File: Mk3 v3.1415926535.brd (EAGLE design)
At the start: 121.6 x 70 mm, 152 parts, among them IC1 TPD3E001DRL, IC2 TPS62082, IC3 STM32F401V, IC4 BQ24092, IC6 CC3100MOD, IC7 BQ2970, IC8 LSM6DS3, IC9 LIS3MDL, J1 ZX62-AB-5PA(11), J2 ER-CON50HT-1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

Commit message: Sponsor logos to rear Note this moves the files to Eagle 7
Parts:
- removed LOGO3: MICROPYTHON-SILK, TiLDA Mk3 Parts:UPYTHON_LOGO_SLIKONLY
- removed U$5: (no value), TiLDA Mk3 Parts:EMFLOGO1
- added U$11: (no value), TiLDA Mk3 Parts:LOGO_MICROPYTHON_8MM
- added U$2: (no value), TiLDA Mk3 Parts:LOGO_MS_4MM
- added U$4: (no value), TiLDA Mk3 Parts:LOGO_ST_4MM
- added U$8: (no value), TiLDA Mk3 Parts:LOGO_TI_4MM
- added U$9: (no value), TiLDA Mk3 Parts:LOGO_HDC_4MM
- moved LOGO1 69.6 mm to (113.9, 49.2)
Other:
- board text added: "Made in the UK"
- board text added: "badge.emfcamp.org/2016"
- board text added: "v3.1415926535"
- board text removed: "MFB"
- board text removed: "Tilda Mk3 Rev.3 May 2016"

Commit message: Lots of clean up in schematic
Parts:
- C27, C5, C6: device passives-7351:C0805-N -> TiLDA Mk3 Parts:C0805-N
- D1: device SparkFun-LED:WS2812B -> TiLDA Mk3 Parts:WS2812B
- D2, D3: device Diodes:SOD123 -> TiLDA Mk3 Parts:SOD123
- IC3: value STM32F401V -> STM32L475VG
- J3: value SWD_SHROUD-PINHEAD -> 2x5 1.27mm
- JP1, JP2: device SparkFun-Connectors:1X11 -> TiLDA Mk3 Parts:1X11
- JP4: device tag-connect:TC2030-MCP-NL -> TiLDA Mk3 Parts:TC2030-MCP-NL
- LED2, LED4, LED5: value RED -> 0603 RED
- LED3: value GREEN -> 0603 GREEN
- LOGO2: value (none) -> LOGO_TI-4MM
- LOGO3: value (none) -> LOGO_ST-4MM
- LOGO4: value (none) -> LOGO_HCD-4MM
- LOGO5: value (none) -> LOGO_MICROSOFT-4MM
- LOGO6: value (none) -> LOGO_MICROPYTHON-8MM
- R7: value DNP or 0 -> DNP or 0603/0R/5%
- S1: value (none) -> 6x3; device SparkFun-Electromechanical:TACTILE-SWITCH-1101NE -> TiLDA Mk3 Parts:TACTILE-SWITCH-1101NE
- S3, S4: value 1217769 -> SKPMAPE010
- S7: value SWITCH-MOMENTARY-2SMD-1101NE -> 6x3; device SparkFun-Electromechanical:TACTILE-SWITCH-1101NE -> TiLDA Mk3 Parts:TACTILE-SWITCH-1101NE
- S8: value DNP -> DNP (6x3); device SparkFun-Electromechanical:TACTILE-SWITCH-1101NE -> TiLDA Mk3 Parts:TACTILE-SWITCH-1101NE
- SJ1: value JUMPER-PAD-2-NOYES_SILK -> SOLDERJUMPERNO; device SparkFun-Passives:PAD-JUMPER-2-NO_YES_SILK -> TiLDA Mk3 Parts:SJ_2S-NO
- renumbered U$11 to LOGO6, U$2 to LOGO5, U$4 to LOGO3, U$8 to LOGO2, U$9 to LOGO4
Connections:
- net BOOT0 renamed BOOT0/JOY_CEN
- net N$1 renamed DRDY
- net N$22 renamed C1
- net N$38 renamed VACP2
- net BTN_MENU: now also S7.P$2; no longer S7.2
- net CC_RST: now also S8.P$1; no longer S8.1
- net GND: now also S1.P$2, S7.P$1, S8.P$2; no longer S1.2, S7.1, S8.2
- net NRST: now also S1.P$1; no longer S1.1
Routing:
- net +3V3: track 547.7 -> 549.9 mm
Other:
- board text added: "designed and assembled in the UK"
- board text removed: "Made in the UK"

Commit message: More clean up
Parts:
- removed U$1: (no value), TiLDA Mk3 Parts:NAME_AREA
- IC6: value CC3100MOD -> CC3100MOD-LWK; device TiLDA Mk3 Parts:CC3100MOD -> TiLDA Mk3 Parts:CC3100MOD-LWK
- SW1: value JOYSTICK_MINI_MULTICOMP -> JOYSTICK_MINI_MULTICOM_NOSILK; device TiLDA Mk3 Parts:JOYSTICK_MULTICOMP -> TiLDA Mk3 Parts:JOYSTICK_MULTICOMP_NOSILK
- moved U2 54.0 mm to (89.2, 19.6), turned to 90 degrees
- moved FID2 31.3 mm to (121.5, 40.0)
- moved FID5 31.3 mm to (121.5, 40.0)
- moved FID3 29.7 mm to (30.0, -2.00)
- moved FID4 29.7 mm to (30.0, -2.00)
- moved FID1 24.7 mm to (71.5, 65.5)
- moved FID6 24.7 mm to (71.5, 65.5)
- moved IC6 12.6 mm to (104.7, 18.1)
- moved TP20 2.62 mm to (83.0, 20.5)
- moved ANT1 1.95 mm to (105.0, 1.60)
- moved R28 1.10 mm to (53.8, 48.1)
- moved Q4 0.91 mm to (52.5, 52.3)
- moved TP3 0.63 mm to (57.8, 38.6)
- moved C48 0.54 mm to (54.1, 58.1)
- moved D3 0.51 mm to (28.9, 46.5)
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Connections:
- net N$13 renamed BAT
- net N$2 renamed SW
- net N$50 renamed COUT
- net N$54 renamed VBAT_SWITCH_CONTROL
- net N$55 renamed DOUT
- net N$63 renamed V-
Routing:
- net GND: track 141.7 -> 131.4 mm
- net V_UNREG: track 350.9 -> 342.3 mm, vias 23 -> 22
- net FET_OUT: track 68.8 -> 72.5 mm
- net I2C_SDA: track 155.9 -> 153.7 mm
- net LCD0: track 50.7 -> 48.5 mm
- net I2C_SCL: track 156.3 -> 154.2 mm
- net N$64: track 15.7 -> 17.4 mm
- net +3V3: track 549.9 -> 548.3 mm
- net CC_RST: track 118.2 -> 119.6 mm
- net COUT: track 9.73 -> 10.9 mm
- net CC_IRQ: track 96.1 -> 95.1 mm
- net LCD_WRX: track 40.4 -> 41.2 mm
- net LCD_RD: track 40.8 -> 40.2 mm
- net SWDAT: track 56.8 -> 57.4 mm
- net BOOT0/JOY_CEN: track 149.0 -> 148.5 mm
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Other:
- board text removed: "MENU"

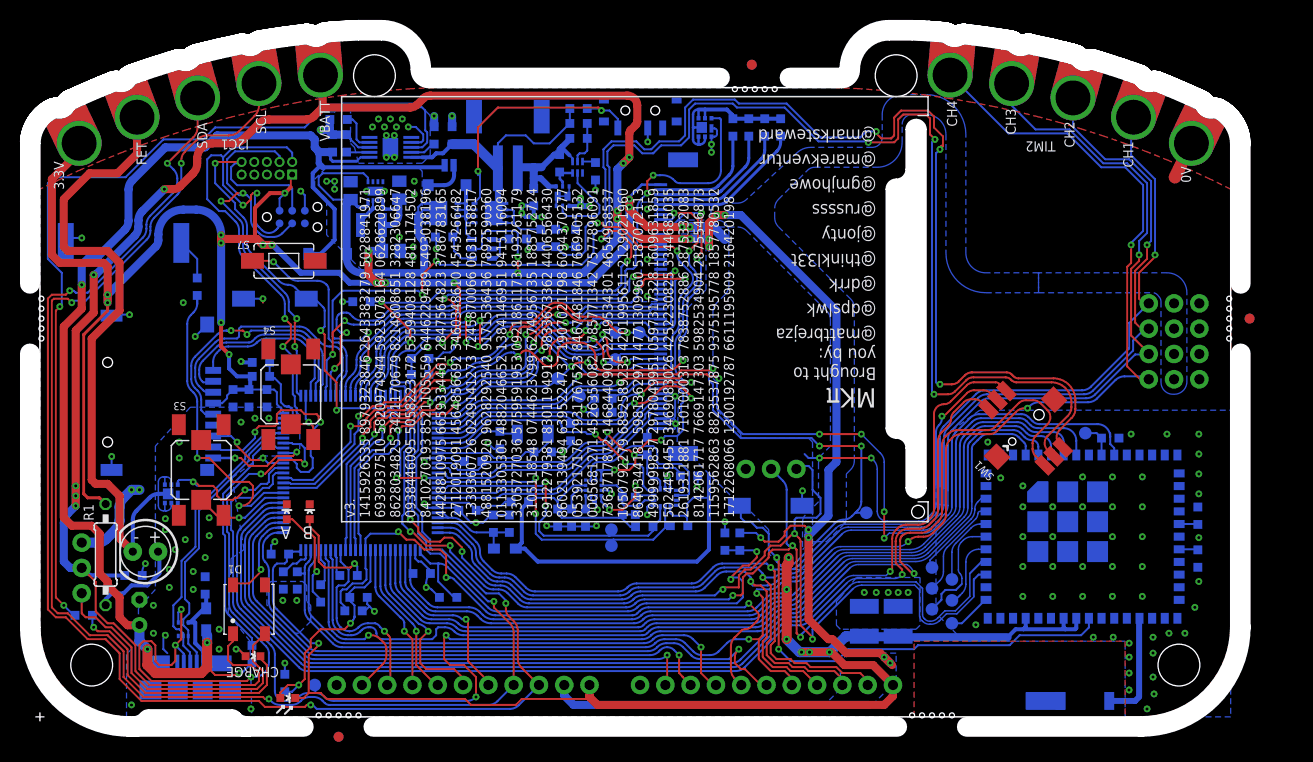
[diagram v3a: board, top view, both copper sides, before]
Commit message: Last footprint change and lots a trace clean up done
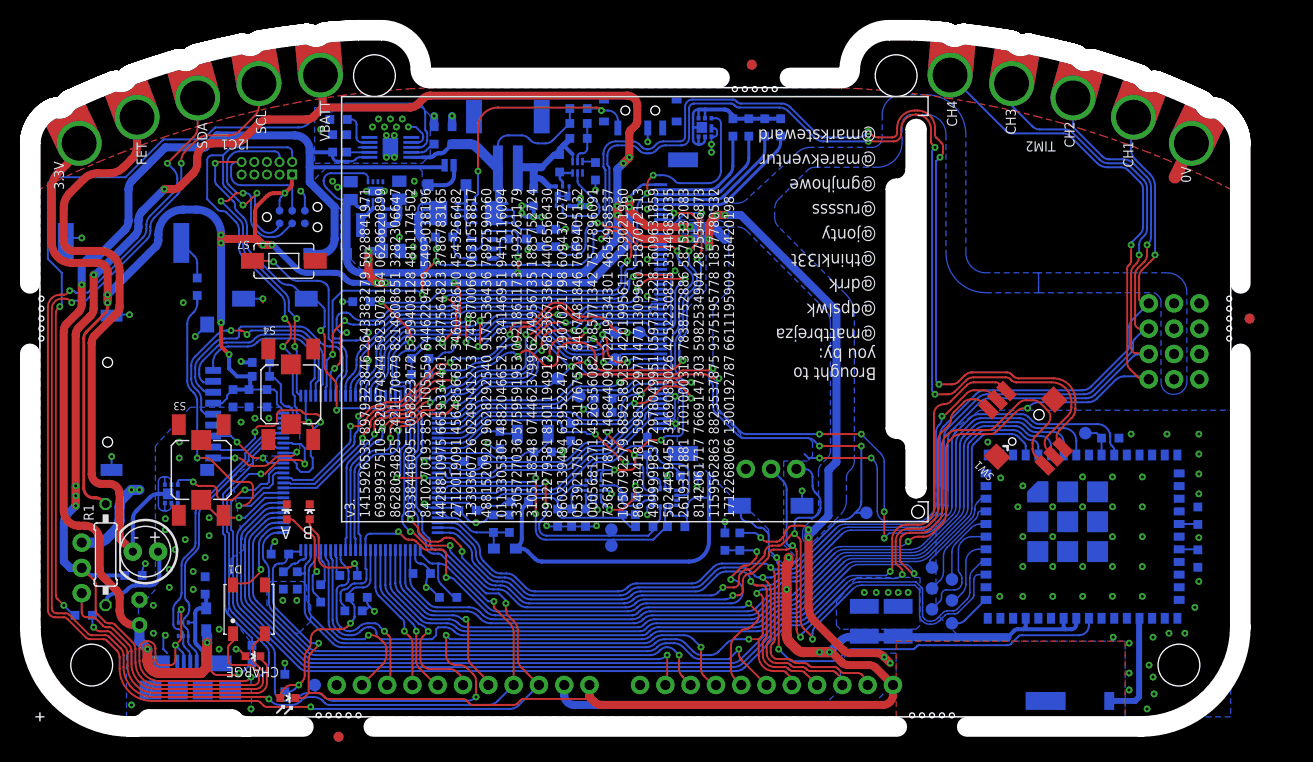
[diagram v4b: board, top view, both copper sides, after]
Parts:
- moved R19 0.32 mm to (63.9, 19.1)
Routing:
- net +3V3: track 548.3 -> 535.3 mm, vias 33 -> 31
- net GND: track 131.4 -> 120.6 mm, vias 154 -> 151
- net V_UNREG: track 342.3 -> 337.2 mm
- net JOY_RIGHT: track 147.2 -> 143.4 mm
- net USART1_RX: track 110.7 -> 107.3 mm
- net BOOT0/JOY_CEN: track 148.5 -> 145.4 mm
- net I2C_SDA: track 153.7 -> 151.2 mm
- net I2C_SCL: track 154.2 -> 151.9 mm
- net VBUS: track 130.6 -> 128.5 mm
- net ADC_VIN: track 50.6 -> 48.9 mm
- net FET_OUT: track 72.5 -> 70.8 mm
- net USART1_TX: track 108.5 -> 106.9 mm
- net LCD2: track 52.4 -> 50.8 mm
- net SCX: track 9.06 -> 10.5 mm
- net VBATT_IN: track 64.2 -> 62.9 mm
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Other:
- board text removed: "MKπ"
- board text removed: "TiLDA"
- board text removed: "v3.1415926535"

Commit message: Last trace touch up's.
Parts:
- moved C7 0.10 mm to (16.7, 13.2)
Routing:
- net +3V3: track 535.3 -> 530.9 mm
- net N$9: track 91.3 -> 90.5 mm
- net CC_HIB: track 128.8 -> 128.2 mm
- net I2C_SCL: track 151.9 -> 151.4 mm
- net VBUS: track 128.5 -> 128.0 mm
